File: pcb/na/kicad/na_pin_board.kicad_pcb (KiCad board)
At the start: 2 copper layers, 14 x 12 mm, 4 parts, among them J1 +5V pin, J2 GND pin, P1 +5V post, P2 GND post

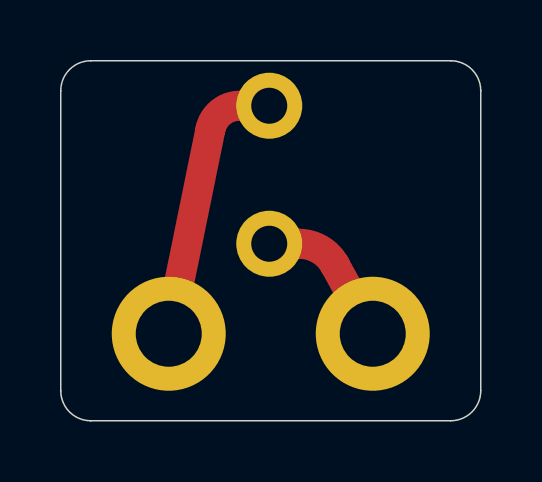
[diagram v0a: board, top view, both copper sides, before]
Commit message: v0.6: one barrier per variant, EU ridges, NA cable slit, ElegooSlicer projects, back cover and plate fixes (D-127..D-150)
- One barrier per variant for every edition; printed blank board in switch only (D-127..D-131)
- EU pin board ridge loop and blank board ridge; more pin board bosses (D-128..D-133)
- NA face plate lobes round the screws form the pocket's ends (D-132)
- NA 5 V cable straight from J2 to J1 through a slit in the barrier's bottom wall, 50 mm FFC; MH3 back in line;
  slit open in battery-free and switch only (D-134, D-135)
- Back cover: flex pad section 1.5 mm in, rim cut at the bottom end with a 0.08 mm-layer taper, steel plate clips
  solid in the shell, bottom clip lead-in 45 deg, pry notch 1.5 deep (D-136..D-143, D-145, D-147)
- 45 deg chamfer round the remote pocket's mouth (D-139)
- Print projects built with ElegooSlicer 1.5.3.5, overrides also as object settings (D-144)
- EU plain face plate 84.6 x 84.6, plain carrier whole on all sides with the full rim (D-146, D-150)
- Steel piece 1.0 mm thick, recess 1.2 deep (D-148)
- MSR-2 12 mm left, grille on the plate's centre line; ant logos in the sensor boards' lower-left corners (D-149)
- Repo URL github.com/antevens/sladdseg on the boards
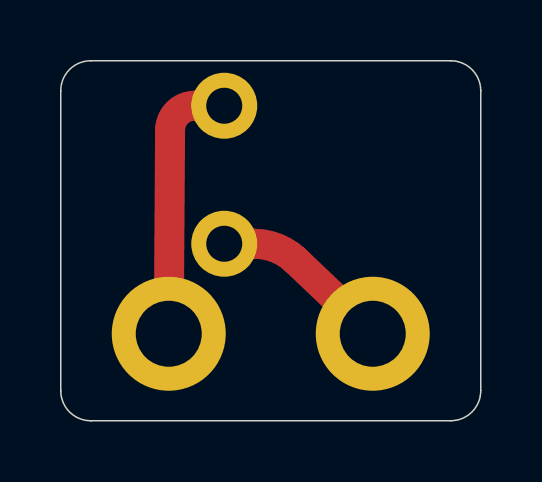
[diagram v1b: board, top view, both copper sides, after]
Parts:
- moved J1 1.50 mm to (111.7, 108.9)
- moved J2 1.50 mm to (111.7, 113.5)
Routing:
- net GND: track 5.05 -> 6.06 mm
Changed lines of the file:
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@@
 	(net 1 "+5V")
 	(net 2 "GND")
+	(footprint "lv:Harwin_P70-2200045"
+		(layer "F.Cu")
+		(at 111.7 113.5)
+		(descr "Harwin P70-2200045 SMT spring pin with peg, pad 2.2 mm, hole 1.2 mm, https://content.harwin.com/asset/7e702b12-8f84-42b5-9282-d7e22f3466f3/DRG-02624-Technical-Drawing-Datasheet-P70-220-pdf.pdf")
+		(tags "spring pin pogo")
+		(property "Reference" "J2"
+			(at 0 0 0)
+			(layer "F.SilkS")
+			(hide yes)
+			(effects
+				(font
+					(size 1 1)
+					(thickness 0.15)
+				)
+			)
+		)
+		(property "Value" "GND pin"
+			(at 0 0 0)
+			(layer "F.Fab")
+			(hide yes)
+			(effects
+				(font
+					(size 1 1)
+					(thickness 0.15)
+				)
+			)
+		)
+		(property "Datasheet" ""
+			(at 0 0 0)
+			(layer "F.Fab")
+			(hide yes)
+			(effects
+				(font
+					(size 1.27 1.27)
+					(thickness 0.15)
+				)
+			)
+		)
+		(property "Description" ""
+			(at 0 0 0)
+			(layer "F.Fab")
+			(hide yes)
+			(effects
+				(font
+					(size 1.27 1.27)
+					(thickness 0.15)
+				)
+			)
+		)
+		(sheetname "Root")
+		(sheetfile "na_pin_board.kicad_sch")
+		(attr smd)
+		(fp_circle
+			(center 0 0)
+			(end 1.35 0)
+			(stroke
+				(width 0.05)
+				(type solid)
+			)
+			(fill no)
+			(layer "F.CrtYd")
+		)
+		(fp_circle
+			(center 0 0)
+			(end 1 0)
+			(stroke
+				(width 0.1)
+				(type solid)
+			)
+			(fill no)
+			(layer "F.Fab")
+		)
+		(pad "1" thru_hole circle
+			(at 0 0)
+			(size 2.2 2.2)
+			(drill 1.2)
+			(layers "*.Cu" "*.Mask" "F.Paste")
+			(remove_unused_layers no)
+			(net 2 "GND")
+		)
+		(embedded_fonts no)
+		(model "${KIPRJMOD}/3d/Harwin_P70-2200045.step"
+			(offset
+				(xyz 0 0 0)
+			)
+			(scale
+				(xyz 1 1 1)
+			)
+			(rotate
+				(xyz 0 0 0)
+			)
+		)
+	)
+	(footprint "lv:M2_Post_Pad_D3.8mm"
+		(layer "F.Cu")
+		(at 116.65 116.5)
+		(descr "M2 screw onto a spacer post: plated 2.2 mm hole, 3.8 mm pad (pan head 4.0)")
+		(tags "M2 post pad")
+		(property "Reference" "P2"
+			(at 0 0 0)
+			(layer "F.SilkS")
+			(hide yes)
+			(effects
+				(font
+					(size 1 1)
+					(thickness 0.15)
+				)
+			)
+		)
+		(property "Value" "GND post"
+			(at 0 0 0)
+			(layer "F.Fab")
+			(hide yes)
+			(effects
+				(font
+					(size 1 1)
+					(thickness 0.15)
+				)
+			)
+		)
+		(property "Datasheet" ""
+			(at 0 0 0)
+			(layer "F.Fab")
+			(hide yes)
+			(effects
+				(font
+					(size 1.27 1.27)
+					(thickness 0.15)
+				)
+			)
+		)
+		(property "Description" ""
+			(at 0 0 0)
+			(layer "F.Fab")
+			(hide yes)
+			(effects
+				(font
+					(size 1.27 1.27)
+					(thickness 0.15)
+				)
+			)
+		)
+		(sheetname "Root")
+		(sheetfile "na_pin_board.kicad_sch")
+		(attr through_hole exclude_from_bom)
+		(fp_circle
+			(center 0 0)
+			(end 2 0)
+			(stroke
+				(width 0.05)
+				(type solid)
+			)
+			(fill no)
+			(layer "F.CrtYd")
+		)
+		(pad "1" thru_hole circle
+			(at 0 0)
+			(size 3.8 3.8)
+			(drill 2.2)
+			(layers "*.Cu" "*.Mask")
+			(remove_unused_layers no)
+			(net 2 "GND")
+		)
+		(embedded_fonts no)
+	)
 	(footprint "lv:M2_Post_Pad_D3.8mm"
 		(layer "F.Cu")
@@
 	(footprint "lv:Harwin_P70-2200045"
 		(layer "F.Cu")
-		(at 113.2 113.5)
-		(descr "Harwin P70-2200045 SMT spring pin with peg, pad 2.2 mm, hole 1.2 mm, https://content.harwin.com/asset/7e702b12-8f84-42b5-9282-d7e22f3466f3/DRG-02624-Technical-Drawing-Datasheet-P70-220-pdf.pdf")
-		(tags "spring pin pogo")
-		(property "Reference" "J2"
-			(at 0 0 0)
-			(layer "F.SilkS")
-			(hide yes)
-			(effects
-				(font
-					(size 1 1)
-					(thickness 0.15)
-				)
-			)
-		)
-		(property "Value" "GND pin"
-			(at 0 0 0)
-			(layer "F.Fab")
-			(hide yes)
-			(effects
-				(font
-					(size 1 1)
-					(thickness 0.15)
-				)
-			)
-		)
-		(property "Datasheet" ""
-			(at 0 0 0)
-			(layer "F.Fab")
-			(hide yes)
-			(effects
-				(font
-					(size 1.27 1.27)
-					(thickness 0.15)
-				)
-			)
-		)
-		(property "Description" ""
-			(at 0 0 0)
-			(layer "F.Fab")
-			(hide yes)
-			(effects
-				(font
-					(size 1.27 1.27)
-					(thickness 0.15)
-				)
-			)
-		)
-		(sheetname "Root")
-		(sheetfile "na_pin_board.kicad_sch")
-		(attr smd)
-		(fp_circle
-			(center 0 0)
-			(end 1.35 0)
-			(stroke
-				(width 0.05)
-				(type solid)
-			)
-			(fill no)
-			(layer "F.CrtYd")
-		)
-		(fp_circle
-			(center 0 0)
-			(end 1 0)
-			(stroke
-				(width 0.1)
-				(type solid)
-			)
-			(fill no)
-			(layer "F.Fab")
-		)
-		(pad "1" thru_hole circle
-			(at 0 0)
-			(size 2.2 2.2)
-			(drill 1.2)
-			(layers "*.Cu" "*.Mask" "F.Paste")
-			(remove_unused_layers no)
-			(net 2 "GND")
-		)
-		(embedded_fonts no)
-		(model "${KIPRJMOD}/3d/Harwin_P70-2200045.step"
-			(offset
-				(xyz 0 0 0)
-			)
-			(scale
-				(xyz 1 1 1)
-			)
-			(rotate
-				(xyz 0 0 0)
-			)
-		)
-	)
-	(footprint "lv:Harwin_P70-2200045"
-		(layer "F.Cu")
-		(at 113.2 108.9)
+		(at 111.7 108.9)
 		(descr "Harwin P70-2200045 SMT spring pin with peg, pad 2.2 mm, hole 1.2 mm, https://content.harwin.com/asset/7e702b12-8f84-42b5-9282-d7e22f3466f3/DRG-02624-Technical-Drawing-Datasheet-P70-220-pdf.pdf")
 		(tags "spring pin pogo")
@@
 		)
 	)
-	(footprint "lv:M2_Post_Pad_D3.8mm"
-		(layer "F.Cu")
-		(at 116.65 116.5)
-		(descr "M2 screw onto a spacer post: plated 2.2 mm hole, 3.8 mm pad (pan head 4.0)")
-		(tags "M2 post pad")
-		(property "Reference" "P2"
-			(at 0 0 0)
-			(layer "F.SilkS")
-			(hide yes)
-			(effects
-				(font
-					(size 1 1)
-					(thickness 0.15)
-				)
-			)
-		)
-		(property "Value" "GND post"
-			(at 0 0 0)
-			(layer "F.Fab")
-			(hide yes)
-			(effects
-				(font
-					(size 1 1)
-					(thickness 0.15)
-				)
-			)
-		)
-		(property "Datasheet" ""
-			(at 0 0 0)
-			(layer "F.Fab")
-			(hide yes)
-			(effects
-				(font
-					(size 1.27 1.27)
-					(thickness 0.15)
-				)
-			)
-		)
-		(property "Description" ""
-			(at 0 0 0)
-			(layer "F.Fab")
-			(hide yes)
-			(effects
-				(font
-					(size 1.27 1.27)
-					(thickness 0.15)
-				)
-			)
-		)
-		(sheetname "Root")
-		(sheetfile "na_pin_board.kicad_sch")
-		(attr through_hole exclude_from_bom)
-		(fp_circle
-			(center 0 0)
-			(end 2 0)
-			(stroke
-				(width 0.05)
-				(type solid)
-			)
-			(fill no)
-			(layer "F.CrtYd")
-		)
-		(pad "1" thru_hole circle
-			(at 0 0)
-			(size 3.8 3.8)
-			(drill 2.2)
-			(layers "*.Cu" "*.Mask")
-			(remove_unused_layers no)
-			(net 2 "GND")
-		)
-		(embedded_fonts no)
-	)
 	(gr_line
 		(start 106.25 108.4)
@@
 	)
 	(segment
+		(start 110.71 108.9)
+		(end 111.7 108.9)
+		(width 1)
+		(layer "F.Cu")
+		(net 1)
+	)
+	(segment
 		(start 109.85 116.5)
-		(end 111.238134 109.693662)
+		(end 109.894671 109.709982)
 		(width 1)
 		(layer "F.Cu")
 		(net 1)
 	)
-	(segment
-		(start 112.21 108.9)
-		(end 113.2 108.9)
+	(arc
+		(start 109.894671 109.709982)
+		(mid 110.135362 109.136916)
+		(end 110.71 108.9)
 		(width 1)
 		(layer "F.Cu")
 		(net 1)
-	)
-	(arc
-		(start 111.238134 109.693662)
-		(mid 111.58262 109.123624)
-		(end 112.21 108.9)
-		(width 1)
-		(layer "F.Cu")
-		(net 1)
-	)
-	(segment
-		(start 114.19 113.5)
-		(end 113.2 113.5)
-		(width 1)
-		(layer "F.Cu")
-		(net 2)
 	)
 	(segment
 		(start 116.65 116.5)
-		(end 115.390354 114.209734)
+		(end 114.07931 114.051724)
 		(width 1)
 		(layer "F.Cu")
 		(net 2)
 	)
+	(segment
+		(start 112.7 113.5)
+		(end 111.7 113.5)
+		(width 1)
+		(layer "F.Cu")
+		(net 2)
+	)
 	(arc
-		(start 115.390354 114.209734)
-		(mid 114.887239 113.690707)
-		(end 114.19 113.5)
-		(width 1)
-		(layer "F.Cu")
+		(start 114.07931 114.051724)
+		(mid 113.442781 113.643046)
+		(end 112.7 113.5)
+		(width 1)
+		(layer "F.Cu")

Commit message: Version v0.7 (D-151): boards, fab and PCBWay packs, order upload name and section renders renamed; v0.6 files removed
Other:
- board text added: "PIN v0.7"
- board text removed: "PIN v0.6"
